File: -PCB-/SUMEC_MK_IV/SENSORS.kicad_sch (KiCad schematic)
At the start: 0 parts

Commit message: MK_IV update
Power supp sheet done, mechanical sheet almost done, some changes, updates etc.
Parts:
- added C28, C29: 10uF.shrp, Capacitor_Tantalum_SMD:CP_EIA-3216-18_Kemet-A_Pad1.58x1.35mm_HandSolder, symbol Device:C_Polarized
- added J3, J4, J5: Conn_01x06_Pin, Connector_Molex:Molex_PicoBlade_53398-0671_1x06-1MP_P1.25mm_Vertical, symbol Connector:Conn_01x06_Pin
- added J6, J7, J9: Conn_01x03_Pin, Connector_Molex:Molex_PicoBlade_53398-0371_1x03-1MP_P1.25mm_Vertical, symbol Connector:Conn_01x03_Pin
- added J8: Conn_01x04_Pin, Connector_Molex:Molex_PicoBlade_53398-0471_1x04-1MP_P1.25mm_Vertical, symbol Connector:Conn_01x04_Pin
- added R14: 10k, Resistor_SMD:R_0805_2012Metric_Pad1.20x1.40mm_HandSolder, symbol Device:R
- added R15: 100, Resistor_SMD:R_0805_2012Metric_Pad1.20x1.40mm_HandSolder, symbol Device:R
- added U6: TSOP382xx, sumec-smdV2_library:TSOP, symbol Interface_Optical:TSOP382xx
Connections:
- new net: J9.2 (Pin_2), R15.2
- new net +3V3: C28.1, C29.1, J6.2 (Pin_2), J7.2 (Pin_2), J8.3 (Pin_3), R14.1, R15.1, U6.3 (Vs)
- new net +5V: J3.1 (Pin_1), J4.1 (Pin_1), J5.1 (Pin_1)
- new net GND: C28.2, C29.2, J3.4 (Pin_4), J3.5 (Pin_5), J4.4 (Pin_4), J4.5 (Pin_5), J5.4 (Pin_4), J5.5 (Pin_5), J6.3 (Pin_3), J7.3 (Pin_3), J8.2 (Pin_2), J9.3 (Pin_3), U6.2 (GND)
- new net IR MODULE: U6.1 (OUT)
- new net QRE1113 A: J8.1 (Pin_1)
- new net QRE1113 B: J8.4 (Pin_4)
- new net QRE1113 C: J9.1 (Pin_1), R14.2
- new net SCL: J3.3 (Pin_3), J4.3 (Pin_3), J5.3 (Pin_3)
- new net SDA: J3.2 (Pin_2), J4.2 (Pin_2), J5.2 (Pin_2)
- new net SHARP 1: J6.1 (Pin_1)
- new net SHARP 2: J7.1 (Pin_1)
- no-connect marks 0 -> 3
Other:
- note added: "DISTANCE SENSORS"
- note added: "DISTANCE SENSORS - SIDE"
- note added: "Digital distance sensor - Sharp GP2Y0D810Z0F"
- note added: "INSPECTED"
- note added: "IR LED Reciver module Operating voltage: 2.7V to 5.5V Frequency: 38kHz High immunity against ambient light. For more than 1 input use - Hexadecimal code Used as a main program starter"
- note added: "IR MODULE"
- note added: "MIRRORED"
- note added: "Miniature Reflective Object Sensor - QRE1113 IR reflectance sensor is comprised of two parts - an IR emitting LED and an IR sensitive phototransistor. Analog output A 100Ω resistor is placed in series with the LED to limit current. A 10kΩ resistor pulls the output pin high, but when the light from the LED is reflected back onto the phototransistor the output will begin to go lower. 2 front sensor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"
- note added: "Sensor detects objects between 2 cm and 10 cm Low when detecting an object, high otherwise. Frequency - 390 Hz Operating voltage 2.7V - 6.2V"
- note added: "TESTED - WORKS, INSPECTED"
- note added: "TF-LUNA MANUAL"
- note added: "Time-of-Flight(ToF) laser-ranging module - TF-Luna COMMUNICATION PROTOCOL: I²C"
- note added: "When pin 5 is connected to ground, TF-Luna enters I2C mode, then its pin 2 is used as SDA data and pin 3 is the SCL clock sending data. Addresses are saved using Nat Simak's program."
- note added: "conn molex 4pin picoblade pro zadni QRE, 2 conn 1. pro predni board, a 2. pro samostatni qre."

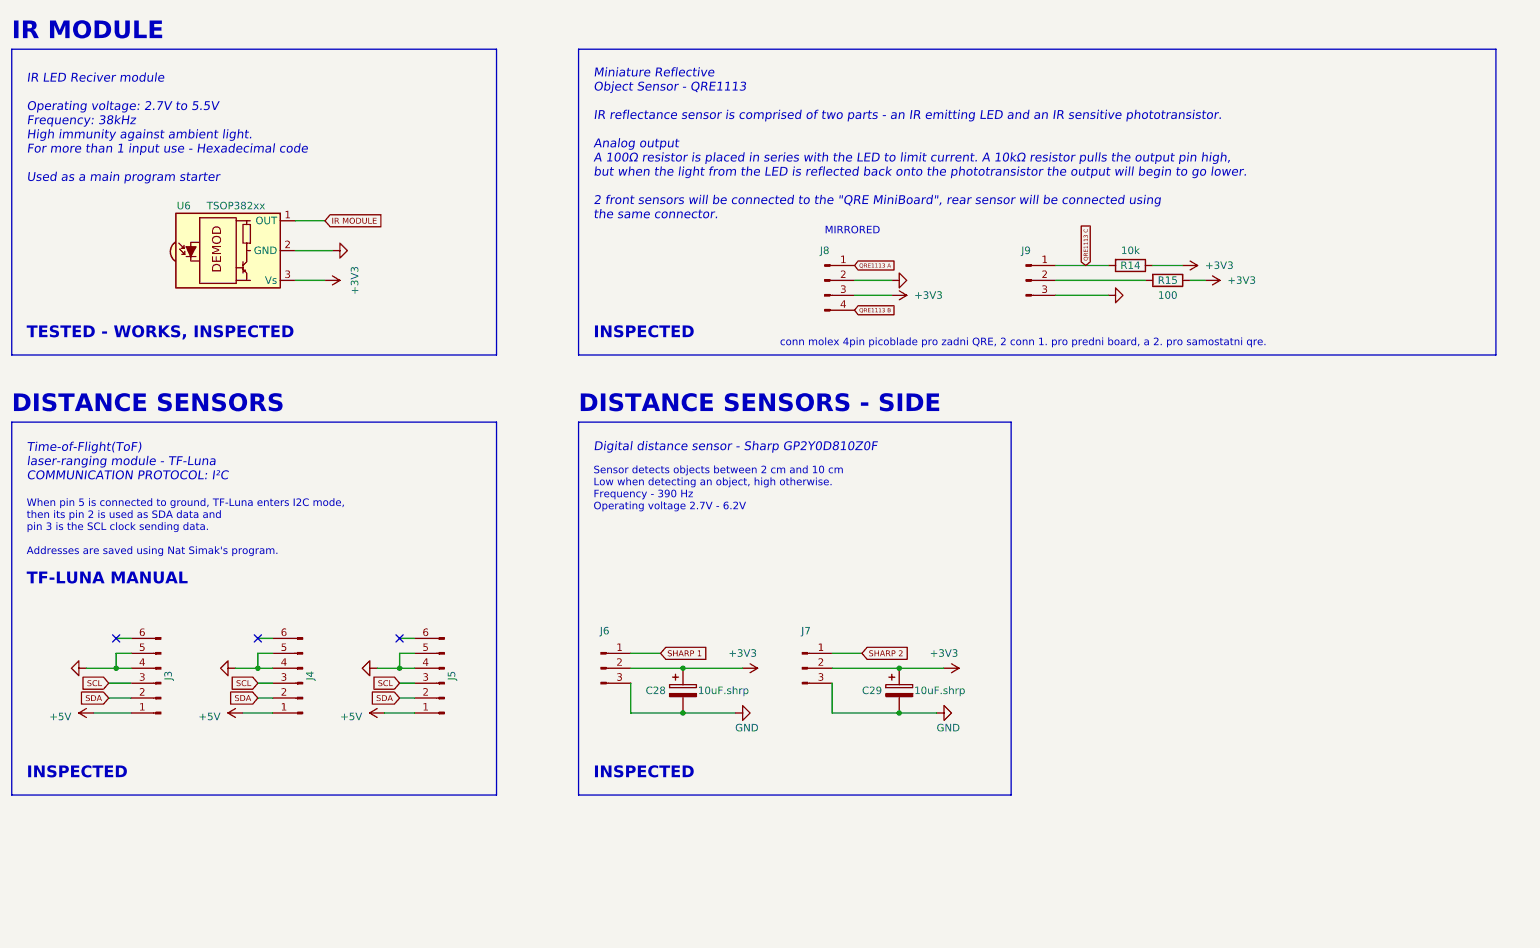
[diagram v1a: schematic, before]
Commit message: MK4 schematic update
Almost done. Did some work on motor drivers, should be final now. Sensors sheet is almost done - object detecting missing. MCU sheet - missing. but yeah. almost done.
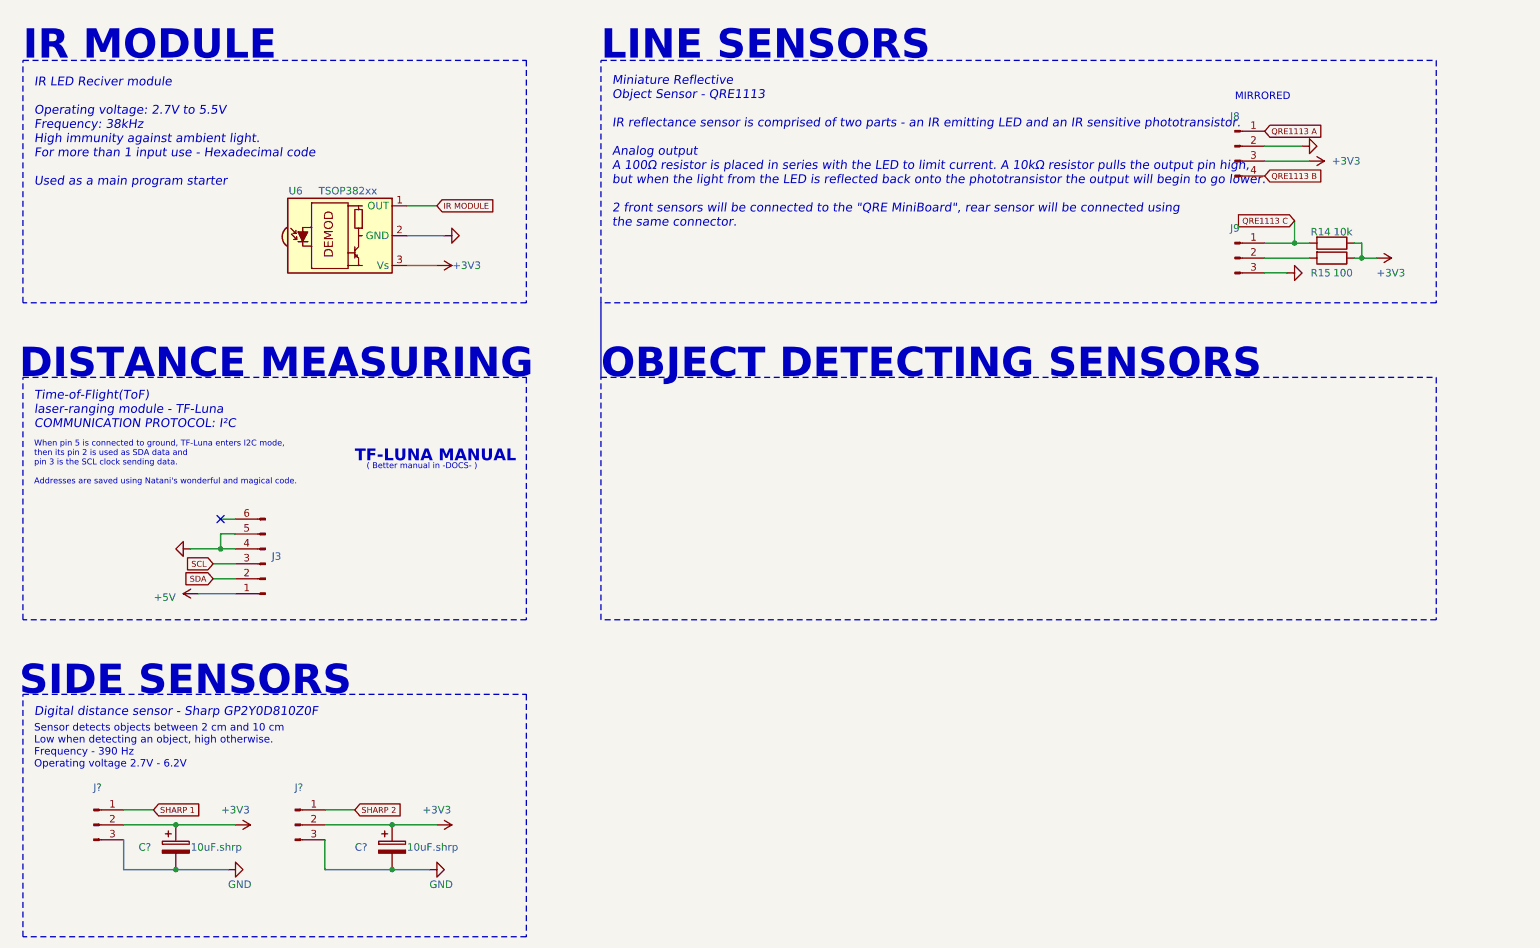
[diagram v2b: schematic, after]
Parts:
- removed C28, C29: 10uF.shrp, Capacitor_Tantalum_SMD:CP_EIA-3216-18_Kemet-A_Pad1.58x1.35mm_HandSolder, symbol Device:C_Polarized
- removed J4, J5: Conn_01x06_Pin, Connector_Molex:Molex_PicoBlade_53398-0671_1x06-1MP_P1.25mm_Vertical, symbol Connector:Conn_01x06_Pin
- removed J6, J7: Conn_01x03_Pin, Connector_Molex:Molex_PicoBlade_53398-0371_1x03-1MP_P1.25mm_Vertical, symbol Connector:Conn_01x03_Pin
- added C? (x2): 10uF.shrp, Capacitor_Tantalum_SMD:CP_EIA-3216-18_Kemet-A_Pad1.58x1.35mm_HandSolder, symbol Device:C_Polarized
- added J? (x2): Conn_01x03_Pin, Connector_Molex:Molex_PicoBlade_53398-0371_1x03-1MP_P1.25mm_Vertical, symbol Connector:Conn_01x03_Pin
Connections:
- net +3V3: now also C?.1, C?.1, J?.2 (Pin_2), J?.2 (Pin_2)
- net GND: now also C?.2, C?.2, J?.3 (Pin_3), J?.3 (Pin_3)
- net SHARP 1: now also J?.1 (Pin_1)
- net SHARP 2: now also J?.1 (Pin_1)
- no-connect marks 3 -> 1
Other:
- note added: "( Better manual in -DOCS- )"
- note added: "DISTANCE MEASURING"
- note added: "LINE SENSORS"
- note added: "OBJECT DETECTING SENSORS"
- note added: "SIDE SENSORS"
- note added: "When pin 5 is connected to ground, TF-Luna enters I2C mode, then its pin 2 is used as SDA data and pin 3 is the SCL clock sending data. Addresses are saved using Natani's wonderful and magical code."
- note removed: "DISTANCE SENSORS"
- note removed: "DISTANCE SENSORS - SIDE"
- note removed: "INSPECTED"
- note removed: "TESTED - WORKS, INSPECTED"
- note removed: "When pin 5 is connected to ground, TF-Luna enters I2C mode, then its pin 2 is used as SDA data and pin 3 is the SCL clock sending data. Addresses are saved using Nat Simak's program."
- note removed: "conn molex 4pin picoblade pro zadni QRE, 2 conn 1. pro predni board, a 2. pro samostatni qre."
- moved on the sheet: J3, J8, J9, R14, R15, U6

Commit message: MKIV update
Updated sensors sheet, did some research, updated mcu. Almoooost done. Gotta take a walk with da dog.
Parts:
- added J? (x2): Conn_01x06_Pin, Connector_Molex:Molex_PicoBlade_53398-0671_1x06-1MP_P1.25mm_Vertical, symbol Connector:Conn_01x06_Pin
- added J? (x3): Conn_01x03_Pin, symbol Connector:Conn_01x03_Pin
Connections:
- net +3V3: now also J?.2 (Pin_2), J?.2 (Pin_2), J?.2 (Pin_2)
- net +5V: now also J?.1 (Pin_1), J?.1 (Pin_1)
- net GND: now also J?.3 (Pin_3), J?.3 (Pin_3), J?.3 (Pin_3), J?.4 (Pin_4), J?.4 (Pin_4), J?.5 (Pin_5), J?.5 (Pin_5)
- net SCL: now also J?.3 (Pin_3), J?.3 (Pin_3)
- net SDA: now also J?.2 (Pin_2), J?.2 (Pin_2)
- new net POL 1: J?.1 (Pin_1)
- new net POL 2: J?.1 (Pin_1)
- new net POL 3: J?.1 (Pin_1)
- no-connect marks 1 -> 3
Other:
- note added: "OPTIONAL"
- note added: "POLOLU SENSOR MANUAL"
- note added: "Pololu Distance Sensor with Pulse Width Output/Digital Output Small lidar based sensor can report presnece/distance of objects up to (TOTAL MAX 200cm-Digital, 300cm - PWM) Distance is chosen by configurating the jumpers with 0R resistors"

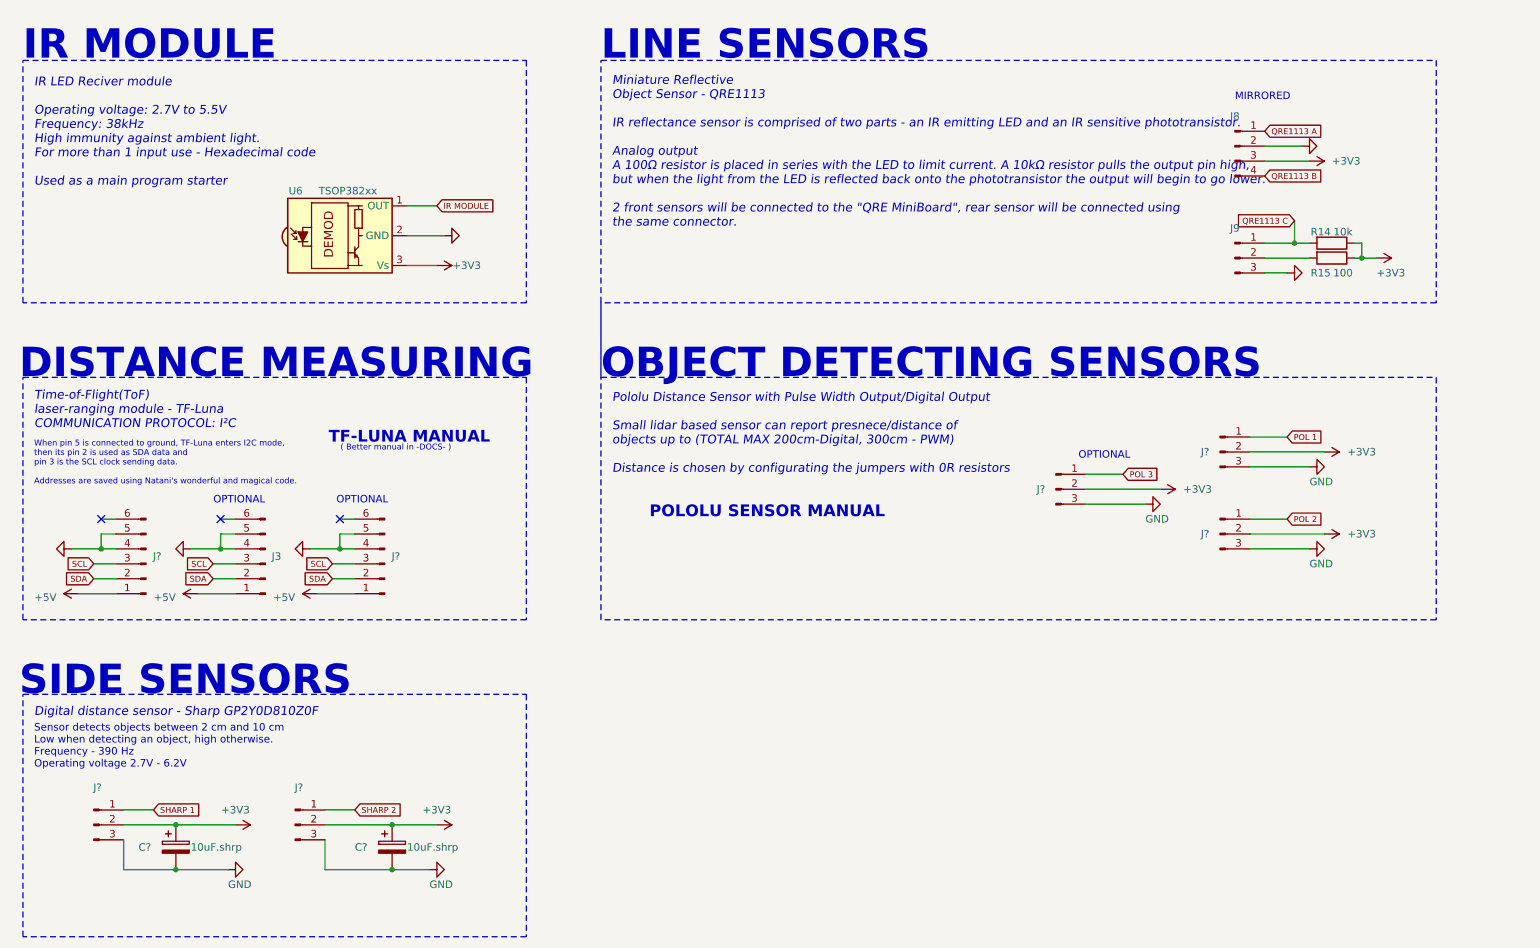
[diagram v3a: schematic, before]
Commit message: MKIV major update
Updated everything, custom symbol for ESP32, MCU sheet done, new test points added, motor control revision.

all left is to clean it up a bit
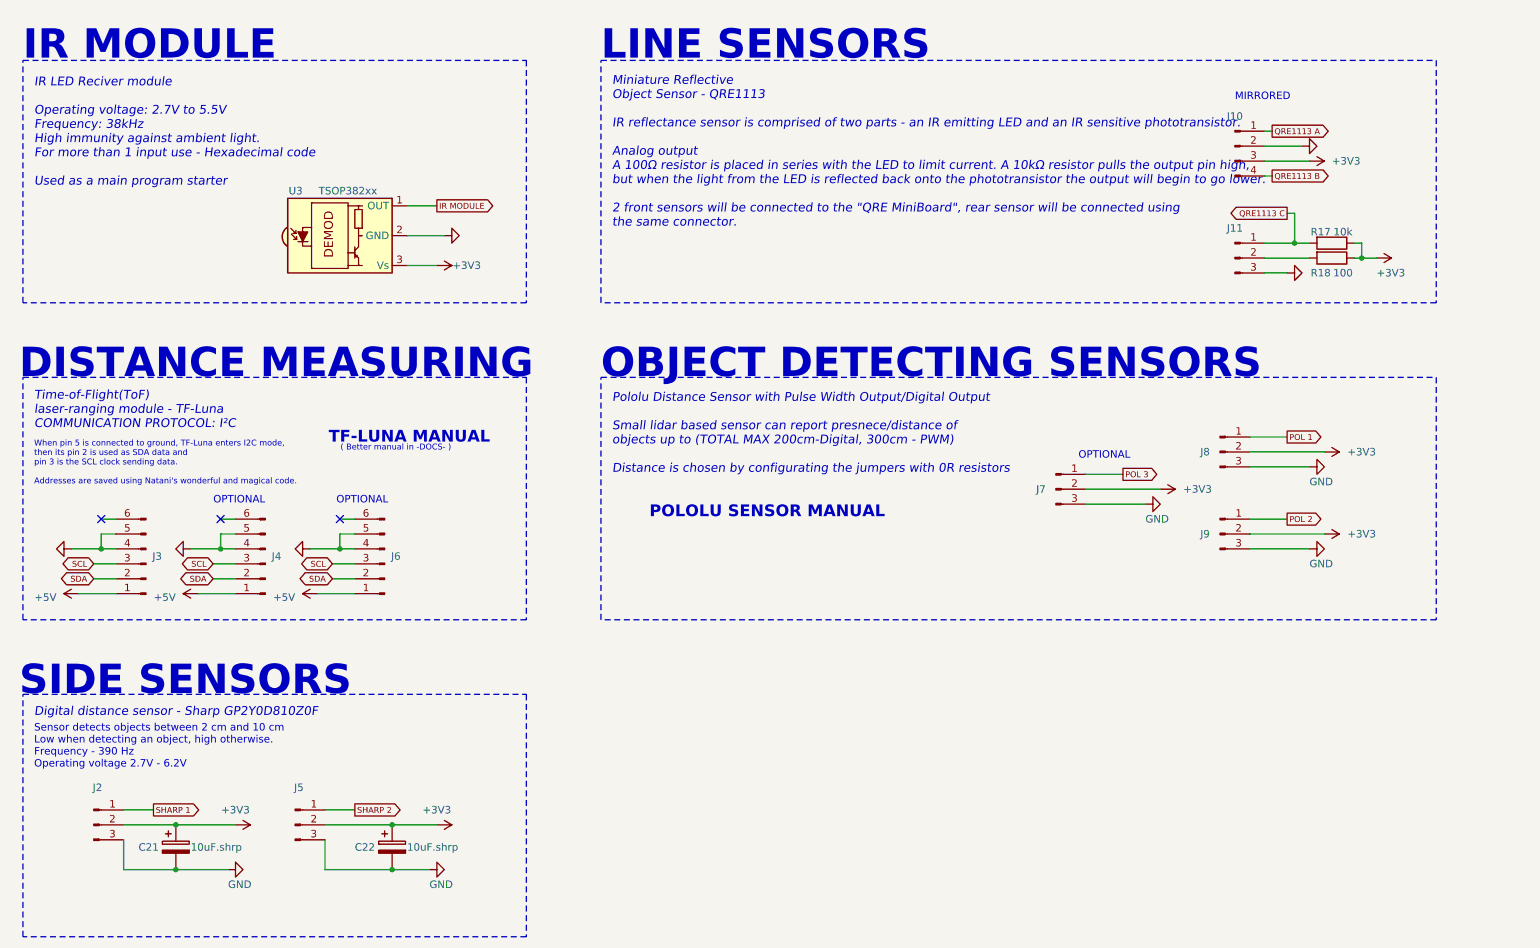
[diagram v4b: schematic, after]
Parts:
- gave numbers to parts that had none: 9
- renumbered J8 to J10, J9 to J11, J3 to J4, R14 to R17, R15 to R18, U6 to U3
